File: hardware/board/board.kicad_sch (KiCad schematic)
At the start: 50 parts, among them J1 Eurorack_Power, J3 Left, J4 Right, J6 Headphones, U1 MAX97220C, U2 74LVC1G04, U3 TL074, U4 MAX9717B

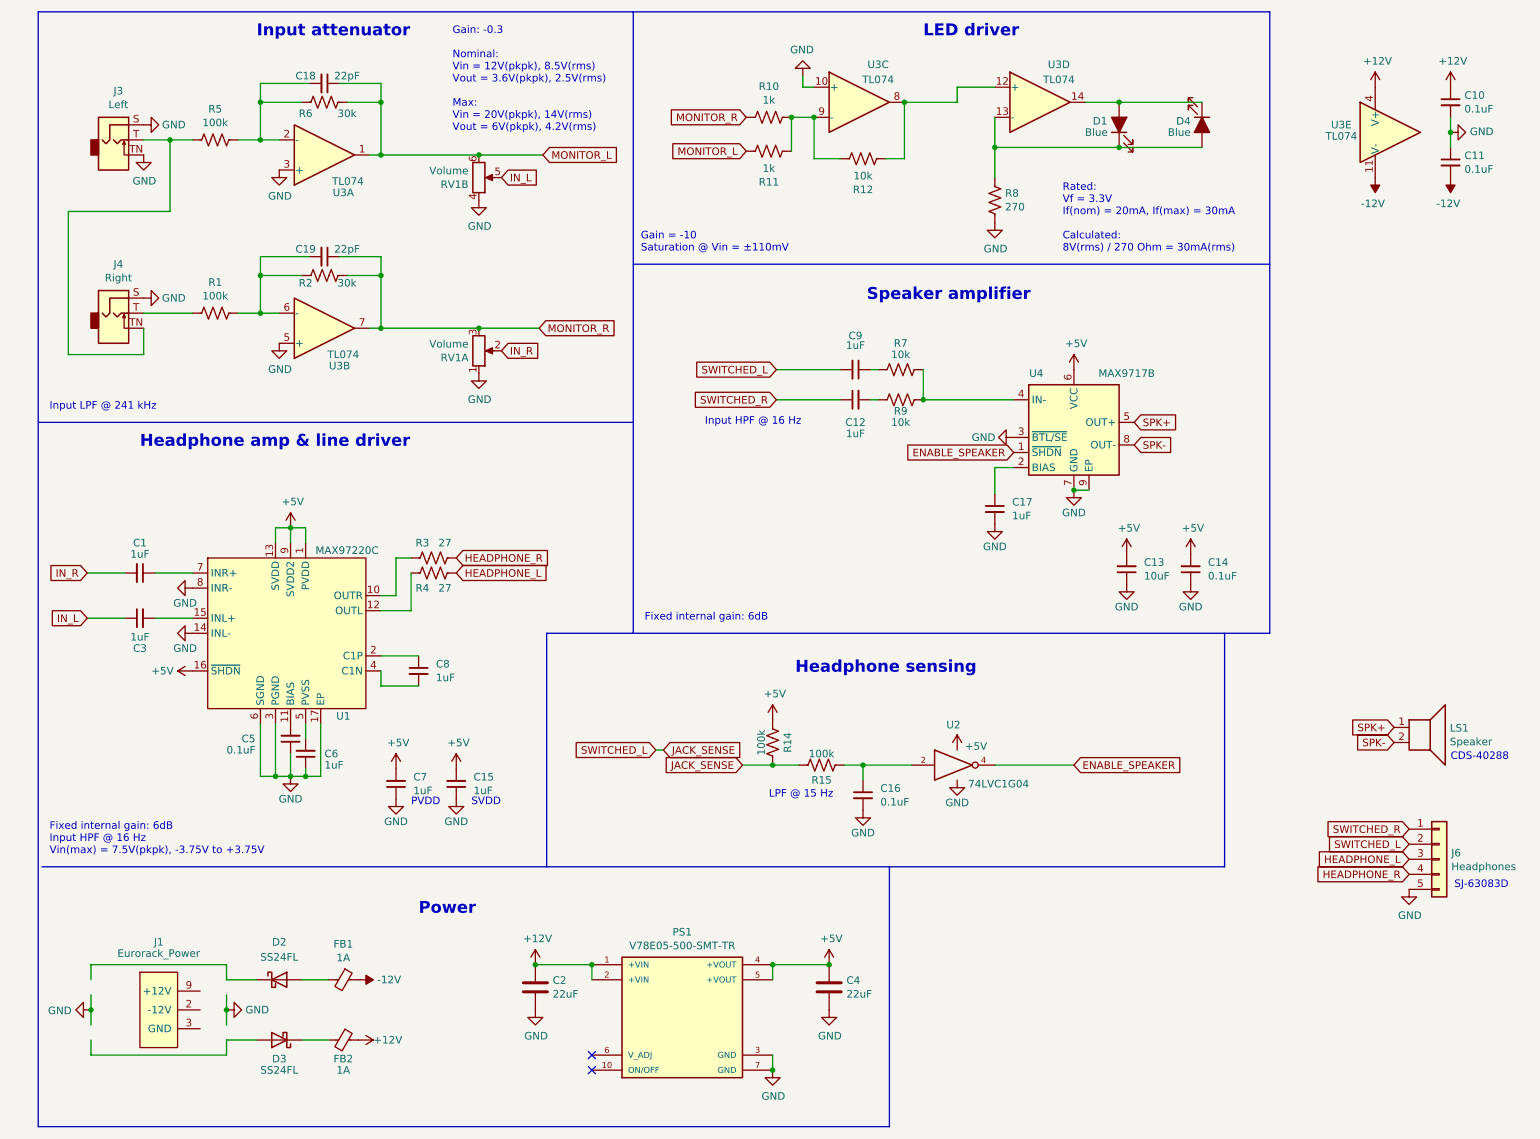
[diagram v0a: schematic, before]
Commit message: hardware: schematic and board revision 9
- Brings page layout and overall style in line with newer Winterbloom projects
- Revised LED driver schematic
- Switched to 4-layer board
- Re-done layout with our newer standards
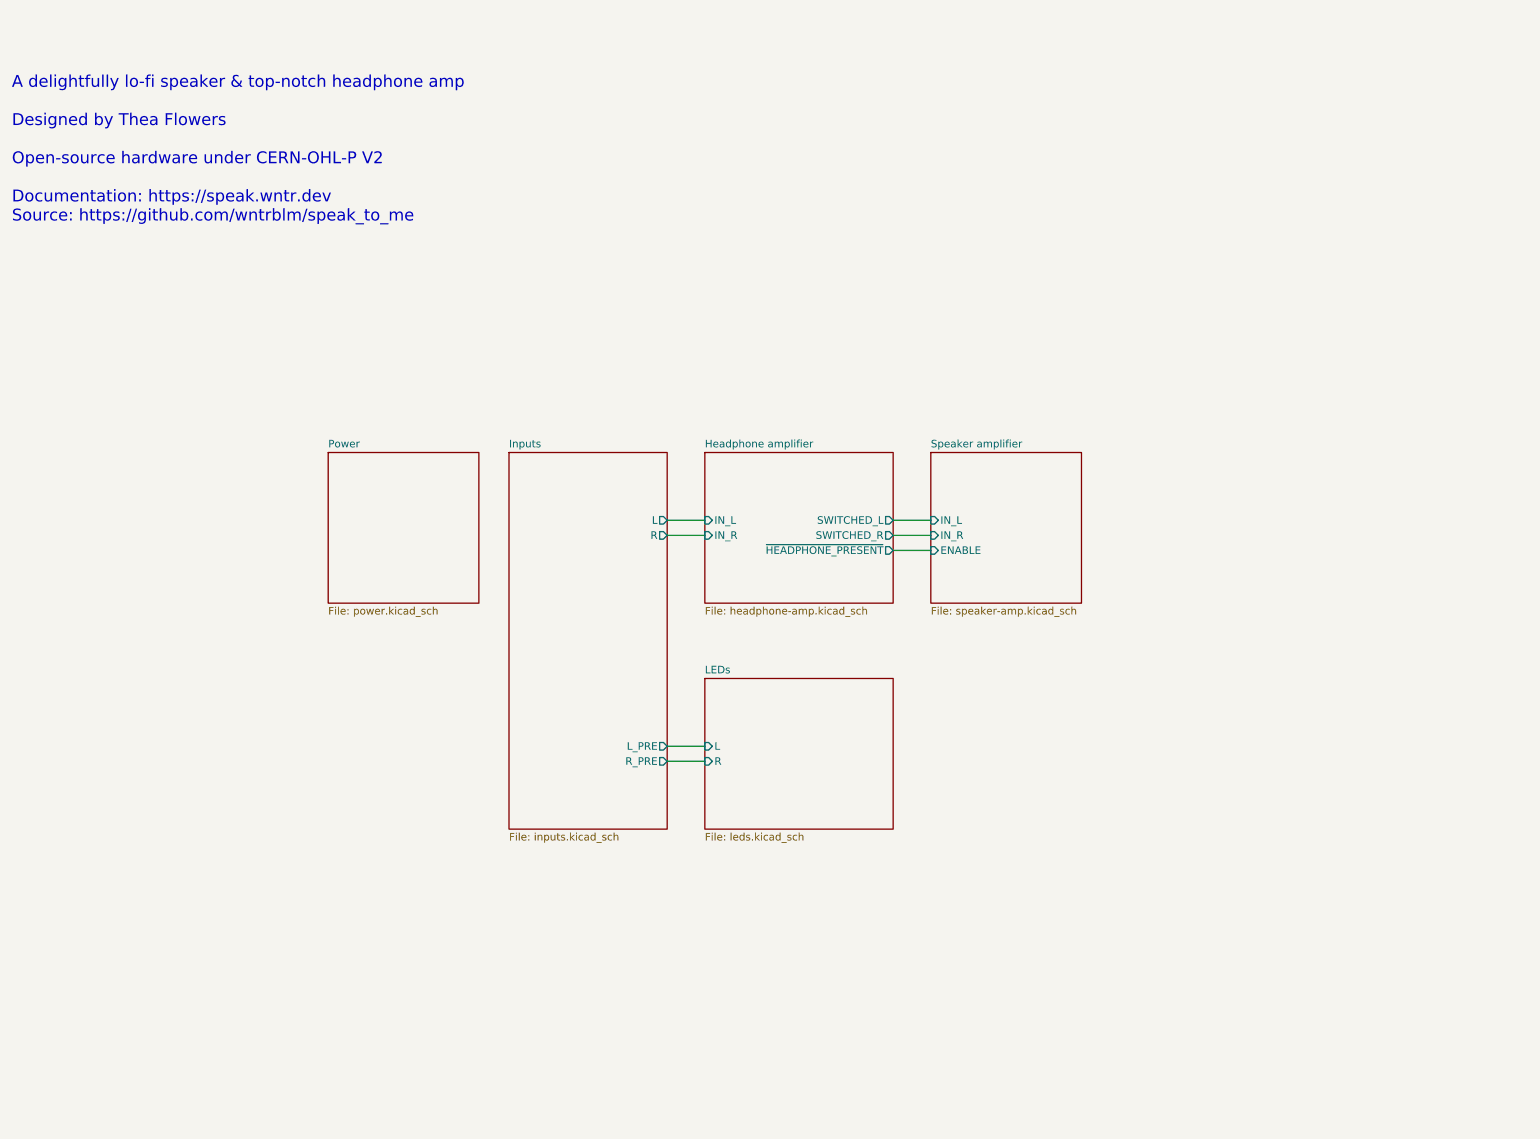
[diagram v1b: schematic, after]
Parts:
- removed C1, C12, C15, C17, C3, C6, C7, C8, C9: 1uF, Capacitor_SMD:C_0603_1608Metric_Pad1.05x0.95mm_HandSolder, symbol Device:C_Small
- removed C10, C11, C14, C16, C5: 0.1uF, Capacitor_SMD:C_0603_1608Metric_Pad1.05x0.95mm_HandSolder, symbol Device:C_Small
- removed C13: 10uF, Capacitor_SMD:C_0603_1608Metric_Pad1.05x0.95mm_HandSolder, symbol Device:C_Small
- removed C18, C19: 22pF, Capacitor_SMD:C_0603_1608Metric_Pad1.05x0.95mm_HandSolder, symbol Device:C_Small
- removed C2, C4: 22uF, Capacitor_SMD:C_0805_2012Metric_Pad1.15x1.40mm_HandSolder, symbol Device:C
- removed D1, D4: Blue, LED_SMD:LED_0805_2012Metric_Pad1.15x1.40mm_HandSolder, symbol Device:LED_ALT
- removed D2, D3: SS24FL, Diode_SMD:D_SOD-123, symbol Device:D_Schottky
- removed FB1, FB2: 1A, Inductor_SMD:L_0603_1608Metric_Pad1.05x0.95mm_HandSolder, symbol Device:Ferrite_Bead_Small
- removed J1: Eurorack_Power, winterbloom:Eurorack_Power, symbol winterbloom:Eurorack_Power
- removed J3: Left, winterbloom:WQP-WQP518MA, symbol winterbloom:Eurorack_Mono_Jack
- removed J4: Right, winterbloom:WQP-WQP518MA, symbol winterbloom:Eurorack_Mono_Jack
- removed J6: Headphones, Connector_PinSocket_2.54mm:PinSocket_1x05_P2.54mm_Vertical, symbol Connector_Generic:Conn_01x05
- removed LS1: Speaker, Connector_JST:JST_XH_B2B-XH-A_1x02_P2.50mm_Vertical, symbol Device:Speaker
- removed PS1: V78E05-500-SMT-TR, board:CONV_V78E05-500-SMT-TR, symbol board:V78E05-500-SMT-TR
- removed R1, R14, R15, R5: 100k, Resistor_SMD:R_0603_1608Metric_Pad1.05x0.95mm_HandSolder, symbol Device:R_US
- removed R10, R11: 1k, Resistor_SMD:R_0603_1608Metric_Pad1.05x0.95mm_HandSolder, symbol Device:R_US
- removed R12, R7, R9: 10k, Resistor_SMD:R_0603_1608Metric_Pad1.05x0.95mm_HandSolder, symbol Device:R_US
- removed R2, R6: 30k, Resistor_SMD:R_0603_1608Metric_Pad1.05x0.95mm_HandSolder, symbol Device:R_US
- removed R3, R4: 27, Resistor_SMD:R_0805_2012Metric_Pad1.15x1.40mm_HandSolder, symbol Device:R_US
- removed R8: 270, Resistor_SMD:R_0603_1608Metric_Pad1.05x0.95mm_HandSolder, symbol Device:R_US
- removed RV1: Volume, Potentiometer_THT:Potentiometer_Alpha_RD902F-40-00D_Dual_Vertical, symbol Device:R_POT_Dual_Separate
- removed U1: MAX97220C, Package_DFN_QFN:TQFN-16-1EP_3x3mm_P0.5mm_EP1.23x1.23mm_ThermalVias, symbol board:MAX97220
- removed U2: 74LVC1G04, Package_TO_SOT_SMD:SOT-23-5, symbol 74xGxx:74LVC1G04
- removed U3: TL074, Package_SO:TSSOP-14_4.4x5mm_P0.65mm, symbol winterbloom:TL074
- removed U4: MAX9717B, winterbloom:MAX9717B, symbol winterbloom:MAX9717B_C_D
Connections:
- no-connect marks 2 -> 0
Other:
- added sheet Headphone amplifier (headphone-amp.kicad_sch)
- added sheet Inputs (inputs.kicad_sch)
- added sheet LEDs (leds.kicad_sch)
- added sheet Power (power.kicad_sch)
- added sheet Speaker amplifier (speaker-amp.kicad_sch)
- note added: "A delightfully lo-fi speaker & top-notch headphone amp Designed by Thea Flowers Open-source hardware under CERN-OHL-P V2 Documentation: https://speak.wntr.dev Source: https://github.com/wntrblm/speak_to_me"
- note removed: "CDS-40288"
- note removed: "Fixed internal gain: 6dB"
- note removed: "Fixed internal gain: 6dB Input HPF @ 16 Hz Vin(max) = 7.5V(pkpk), -3.75V to +3.75V"
- note removed: "Gain = -10 Saturation @ Vin = ±110mV"
- note removed: "Gain: -0.3 Nominal: Vin = 12V(pkpk), 8.5V(rms) Vout = 3.6V(pkpk), 2.5V(rms) Max: Vin = 20V(pkpk), 14V(rms) Vout = 6V(pkpk), 4.2V(rms)"
- note removed: "Headphone amp & line driver"
- note removed: "Headphone sensing"
- note removed: "Input HPF @ 16 Hz"
- note removed: "Input LPF @ 241 kHz"
- note removed: "Input attenuator"
- note removed: "LED driver"
- note removed: "LPF @ 15 Hz"
- note removed: "PVDD"
- note removed: "Power"
- note removed: "Rated: Vf = 3.3V If(nom) = 20mA, If(max) = 30mA Calculated: 8V(rms) / 270 Ohm = 30mA(rms)"
- note removed: "SJ-63083D"
- note removed: "SVDD"
- note removed: "Speaker amplifier"
